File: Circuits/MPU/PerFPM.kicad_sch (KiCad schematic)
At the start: 48 parts, among them Q1 SI4421DY, Q2 MMBTA92, Q3 MMBTA92, U3 LT1715, U4 ADA4805-2ARMZ, U5 ADA4805-2ARMZ, U6 ADA4805-2ARMZ

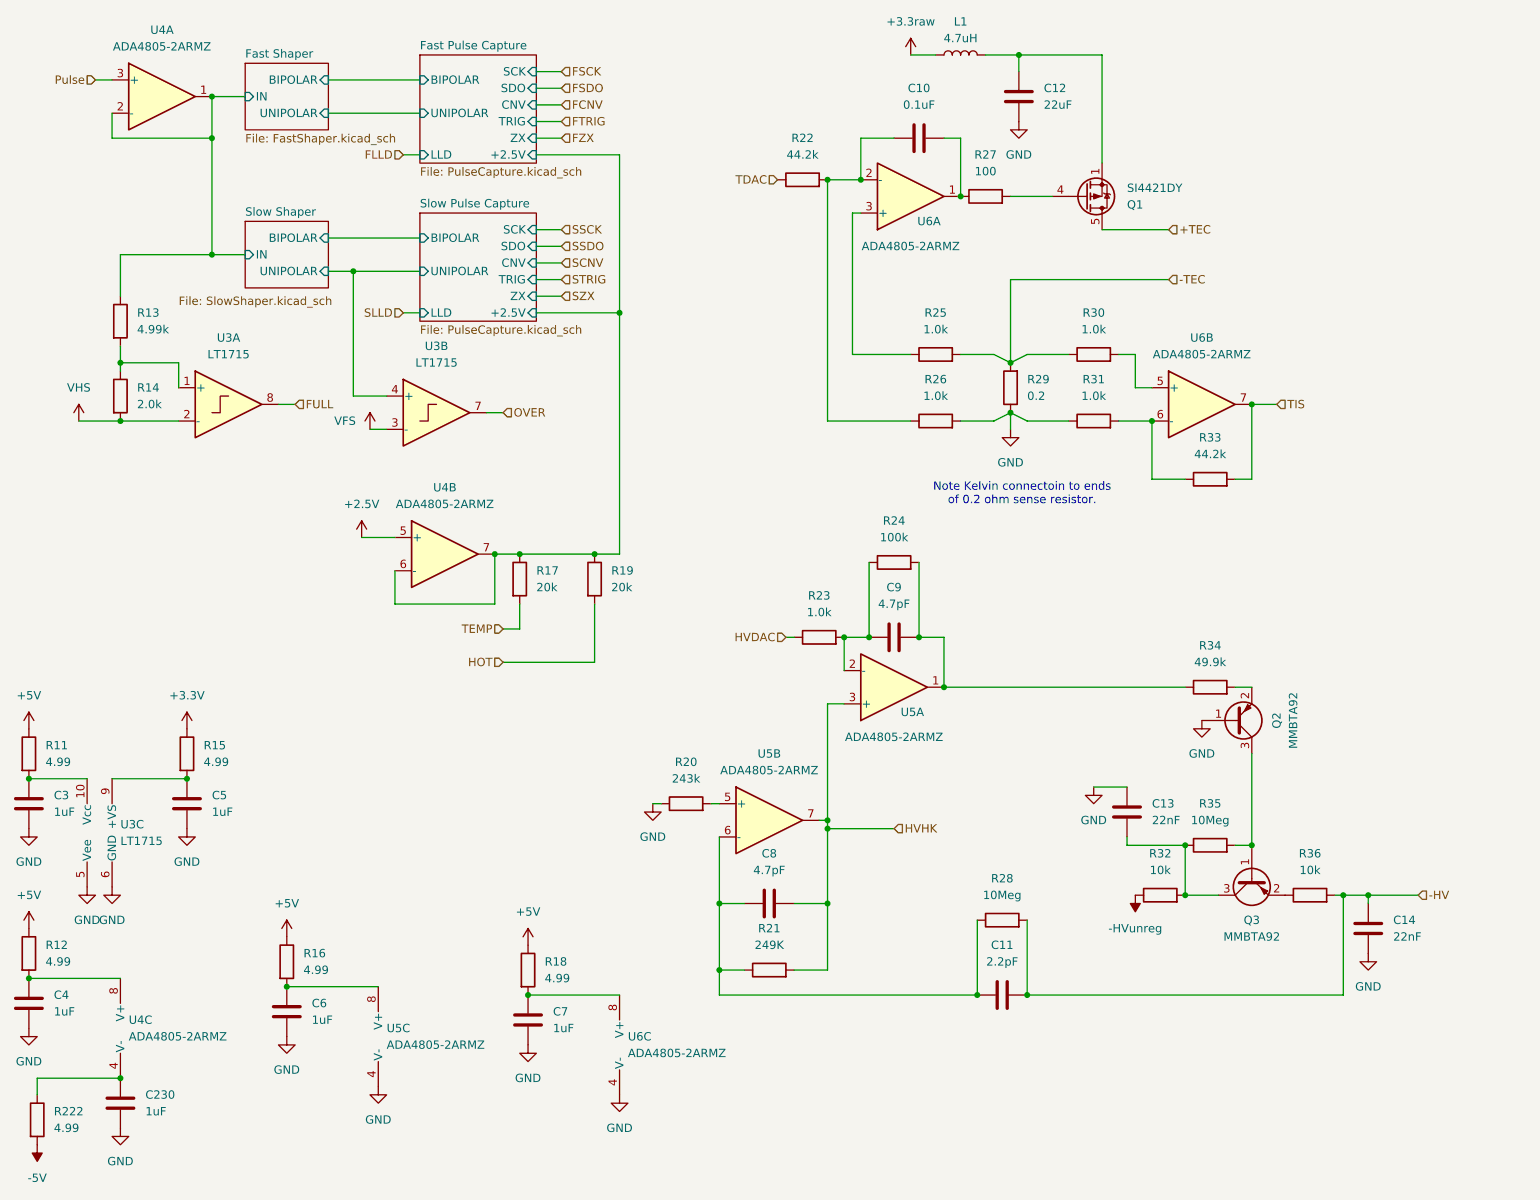
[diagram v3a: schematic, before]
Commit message: S/H for fast channel. Higher HV.
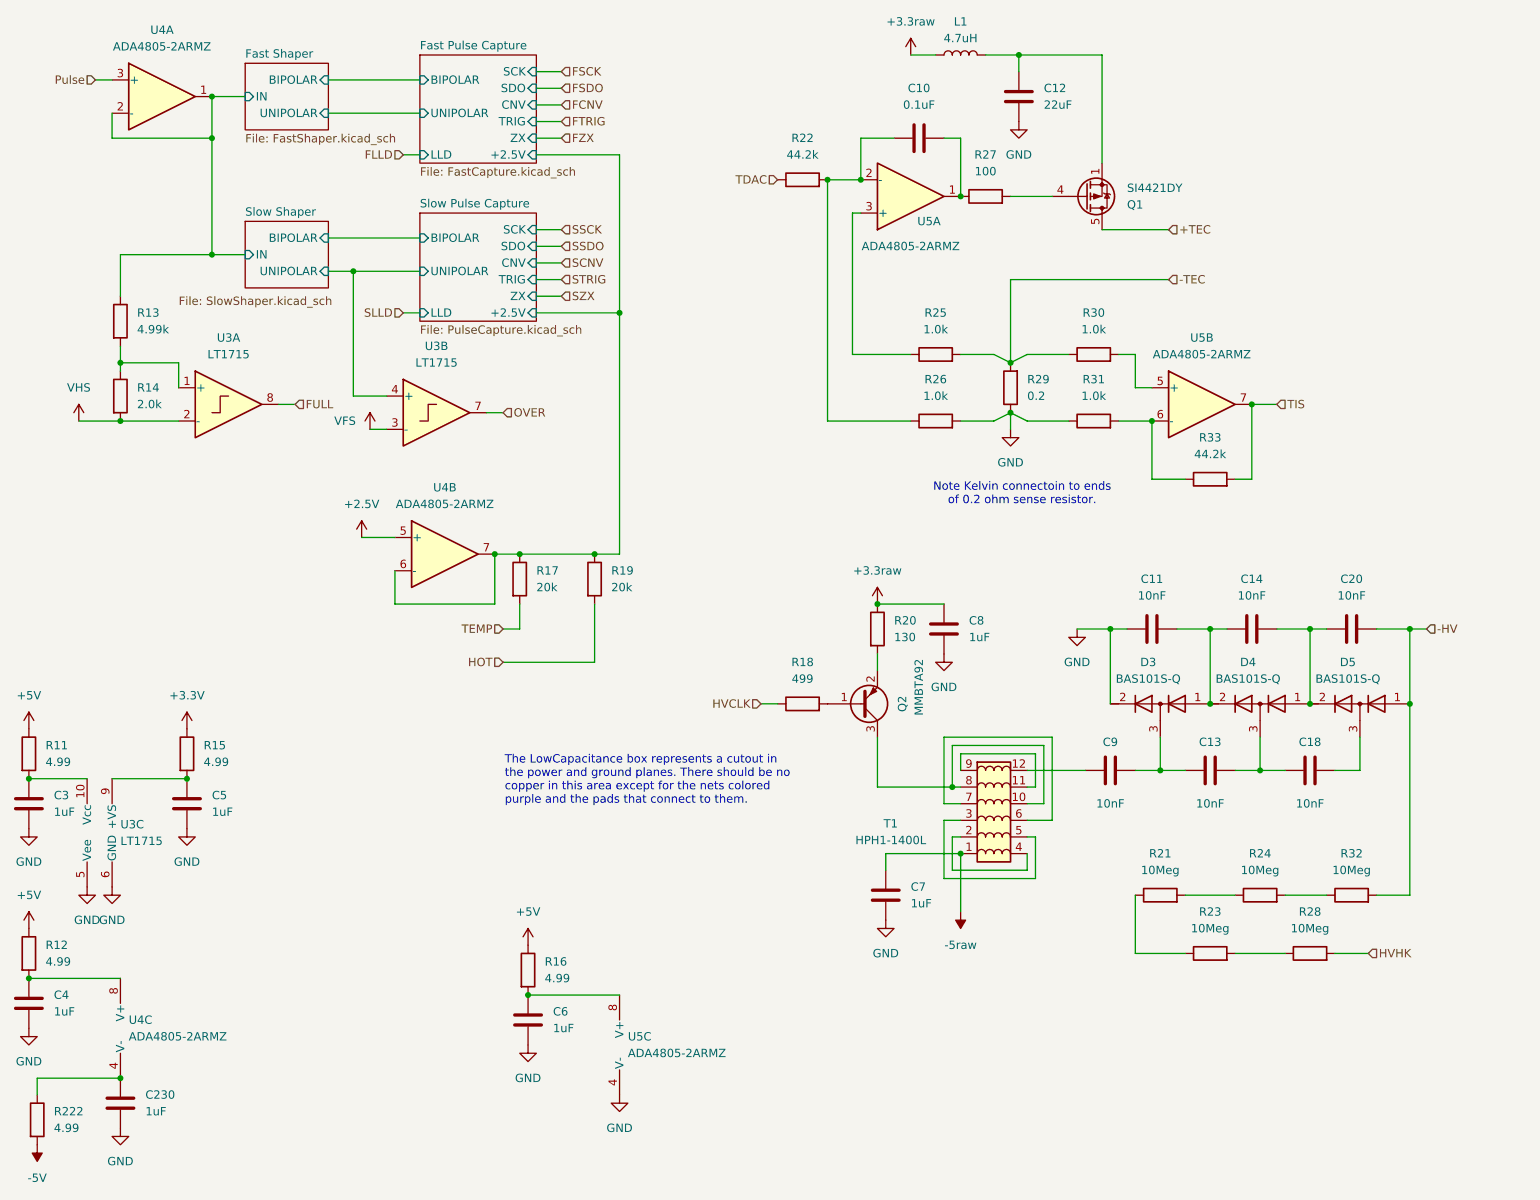
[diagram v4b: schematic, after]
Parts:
- removed C11: 2.2pF, Capacitor_SMD:C_1206_3216Metric, symbol QuERI_symbols:Csmall
- removed C13, C14: 22nF, Capacitor_SMD:C_1210_3225Metric, symbol QuERI_symbols:C
- removed C6: 1uF, Capacitor_SMD:C_0805_2012Metric, symbol QuERI_symbols:C
- removed C8, C9: 4.7pF, Capacitor_SMD:C_0603_1608Metric, symbol QuERI_symbols:Csmall
- removed Q3: MMBTA92, Package_TO_SOT_SMD:SOT-23, symbol Transistor_BJT:MMBTA92
- removed R16: 4.99, Resistor_SMD:R_0603_1608Metric, symbol QuERI_symbols:Rlowp
- removed R20: 243k, Resistor_SMD:R_0603_1608Metric, symbol QuERI_symbols:Rlowp
- removed R34: 49.9k, Resistor_SMD:R_0603_1608Metric, symbol QuERI_symbols:Rlowp
- removed R35: 10Meg, Resistor_SMD:R_2010_5025Metric, symbol QuERI_symbols:Rlowp
- removed R36: 10k, Resistor_SMD:R_0603_1608Metric, symbol QuERI_symbols:Rlowp
- removed U5: ADA4805-2ARMZ, Package_SO:MSOP-8_3x3mm_P0.65mm, symbol QuERI_symbols:ADA4805-2ARMZ
- added C11, C13, C14, C18, C20, C9: 10nF, Capacitor_SMD:C_0603_1608Metric, symbol QuERI:Csmall
- added C7, C8: 1uF, Capacitor_SMD:C_0805_2012Metric, symbol QuERI_symbols:C
- added D3, D4, D5: BAS101S-Q, Package_TO_SOT_SMD:SOT-323_SC-70, symbol QuERI:BAS21SW
- added R18: 499, Resistor_SMD:R_0603_1608Metric, symbol QuERI_symbols:Rlowp
- added R20: 130, Resistor_SMD:R_1206_3216Metric, symbol Device:R
- added T1: HPH1-1400L, symbol QuERI_symbols:Hexapath
- R21: value 249K -> 10Meg; Spec 1% 1/10W -> 1% 1/10W HV
- R23: value 1.0k -> 10Meg; Spec 1% 1/10W -> 1% 1/10W HV
- R24: value 100k -> 10Meg; Spec 1% 1/10W -> 1% 1/10W HV
- R28: footprint Resistor_SMD:R_2010_5025Metric -> Resistor_SMD:R_0603_1608Metric; Spec 1% 1/10W -> 1% 1/10W HV
- R32: value 10k -> 10Meg; Spec 1% 1/10W -> 1% 1/10W HV
- renumbered C7 to C6, R18 to R16, U6 to U5
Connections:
- net -HVunreg is gone; now on an unnamed net: R32.1
- net +3.3raw: now also C8.1, R20.1
- net -HV: now also R32.2, C20.2, D5.1 (A); no longer R28.2
- net GND: now also C11.1, C7.2, C8.2, D3.2 (K); no longer Q2.1 (B)
- net HVHK: now also R28.2; no longer R21.2
- net at R28.1: now also R23.2; no longer R21.1
- net at Q2.2 (E): now also R20.2
- net at R24.1: now also R21.2; no longer R23.2
- net at Q2.3 (C): now also T1.10, T1.8
- net HVDAC: no longer names the net of R23.1
- net HVDAC: now also R21.1
- new net: C9.1, T1.12
- new net: C13.1, C9.2, D3.3 (common)
- new net: Q2.1 (B), R18.2
- new net: C13.2, C18.1, D4.3 (common)
- new net: C18.2, D5.3 (common)
- new net: C14.2, C20.1, D4.1 (A), D5.2 (K)
- new net: C11.2, C14.1, D3.1 (A), D4.2 (K)
- new net: T1.11, T1.9
- new net: T1.2, T1.4
- new net: T1.3, T1.5
- new net: T1.6, T1.7
- new net -5raw: C7.1, T1.1
- new net HVCLK: R18.1
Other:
- sheet Fast Pulse Capture: file PulseCapture.kicad_sch -> FastCapture.kicad_sch
- note added: "The LowCapacitance box represents a cutout in the power and ground planes. There should be no copper in this area except for the nets colored purple and the pads that connect to them."

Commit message: HV generation based on bench testing
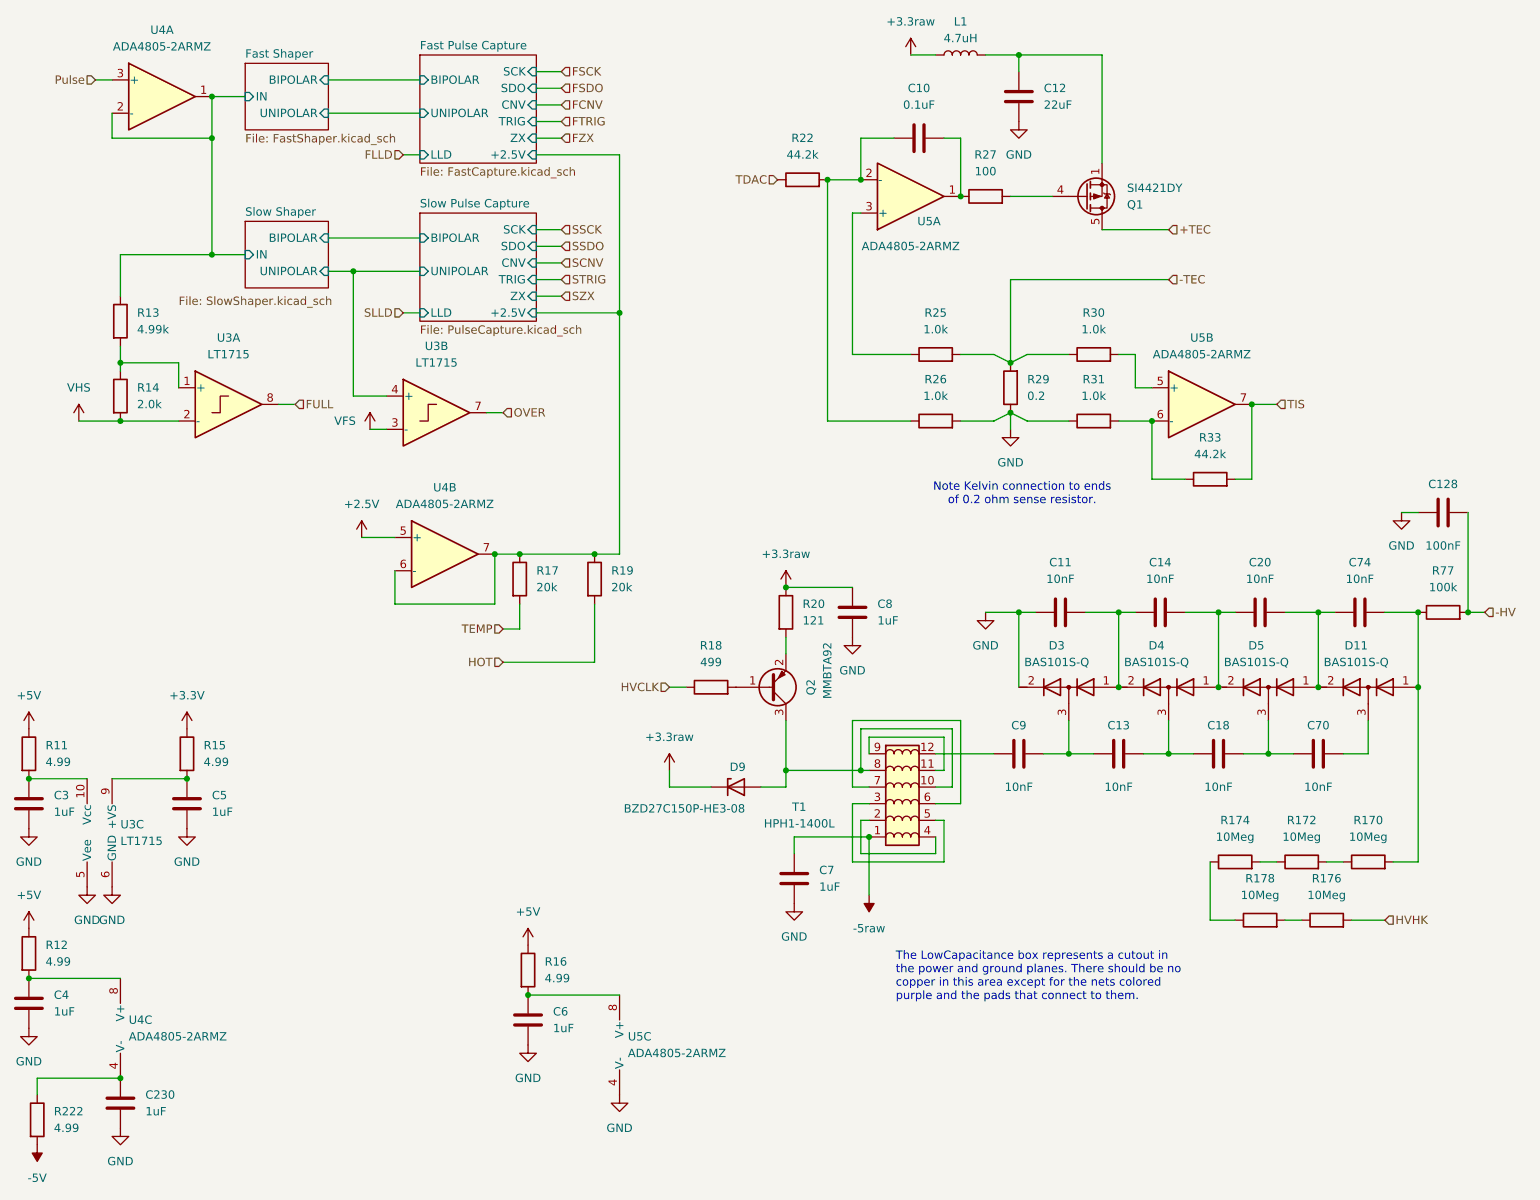
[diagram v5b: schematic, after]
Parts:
- removed R21, R23, R24, R28, R32: 10Meg, Resistor_SMD:R_0603_1608Metric, symbol QuERI_symbols:Rlowp
- added C128: 100nF, Capacitor_SMD:C_1210_3225Metric, symbol QuERI:Csmall
- added C70, C74: 10nF, Capacitor_SMD:C_0603_1608Metric, symbol QuERI:Csmall
- added D11: BAS101S-Q, Package_TO_SOT_SMD:SOT-323_SC-70, symbol QuERI:BAS21SW
- added D9: BZD27C150P-HE3-08, symbol Device:D_Zener
- added R170, R172, R174, R176, R178: 10Meg, Resistor_SMD:R_0603_1608Metric, symbol QuERI_symbols:Rlowp
- added R77: 100k, Resistor_SMD:R_0603_1608Metric, symbol QuERI_symbols:Rlowp
- R20: value 130 -> 121
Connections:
- net +3.3raw: now also D9.1 (K)
- net -HV: now also C128.2, R77.2; no longer C20.2, D5.1 (A)
- net GND: now also C128.1
- net HVHK: now also R176.2
- net at C18.2, D5.3 (common): now also C70.1
- net at Q2.3 (C), T1.10, T1.8: now also D9.2 (A)
- new net: R174.1, R178.1
- new net: R176.1, R178.2
- new net: C20.2, C74.1, D11.2 (K), D5.1 (A)
- new net: C74.2, D11.1 (A), R170.2, R77.1
- new net: R172.1, R174.2
- new net: R170.1, R172.2
- new net: C70.2, D11.3 (common)
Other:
- note added: "Note Kelvin connection to ends of 0.2 ohm sense resistor."
- note removed: "Note Kelvin connectoin to ends of 0.2 ohm sense resistor."
- moved on the sheet: C11, C13, C14, C18, C20, C7, C8, C9, D3, D4, D5, Q2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

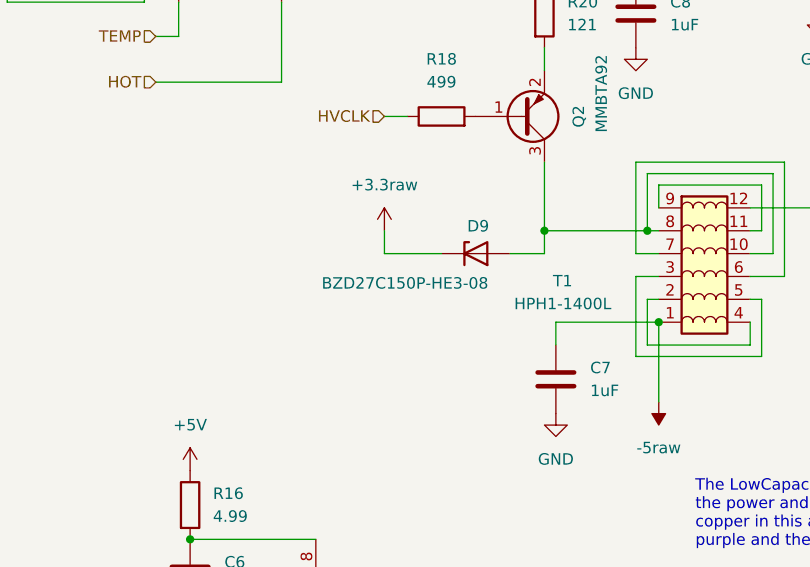
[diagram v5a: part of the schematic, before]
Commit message: more prep for new FPGA
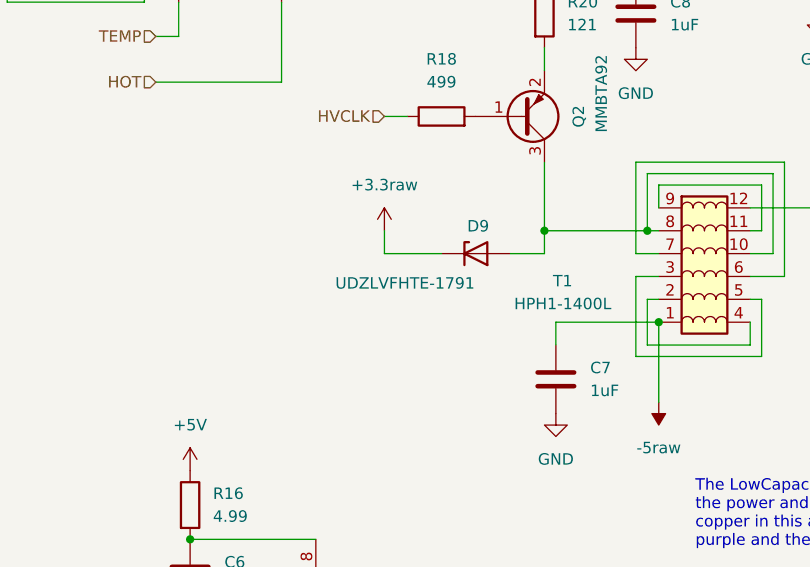
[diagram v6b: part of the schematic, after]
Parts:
- D9: value BZD27C150P-HE3-08 -> UDZLVFHTE-1791; footprint (none) -> Diode_SMD:D_SOD-323F
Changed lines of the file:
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@@
 			)
 		)
-		(property "Value" "BZD27C150P-HE3-08"
+		(property "Value" "UDZLVFHTE-1791"
 			(at 135.636 139.192 0)
 			(effects
@@
 			)
 		)
-		(property "Footprint" ""
+		(property "Footprint" "Diode_SMD:D_SOD-323F"
 			(at 143.51 135.89 0)
 			(effects
